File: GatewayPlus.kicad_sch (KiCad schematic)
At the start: 0 parts

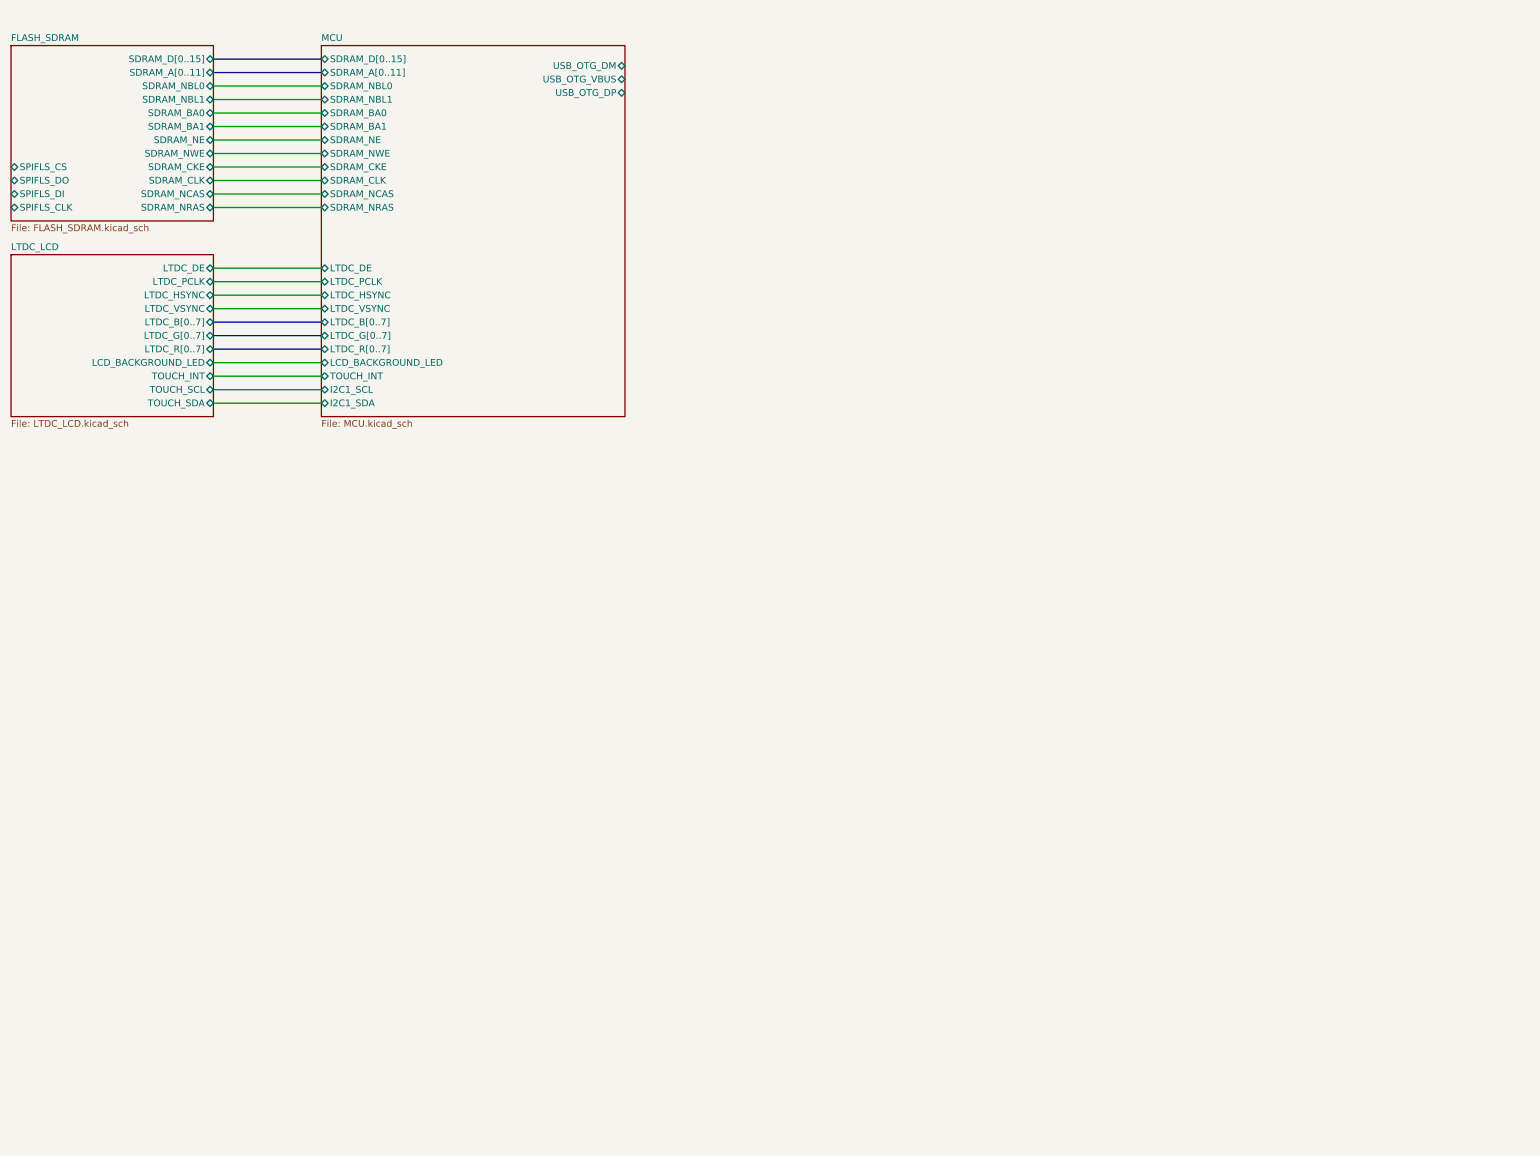
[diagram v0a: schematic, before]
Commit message: Add WiFi block and finished WiFi layout
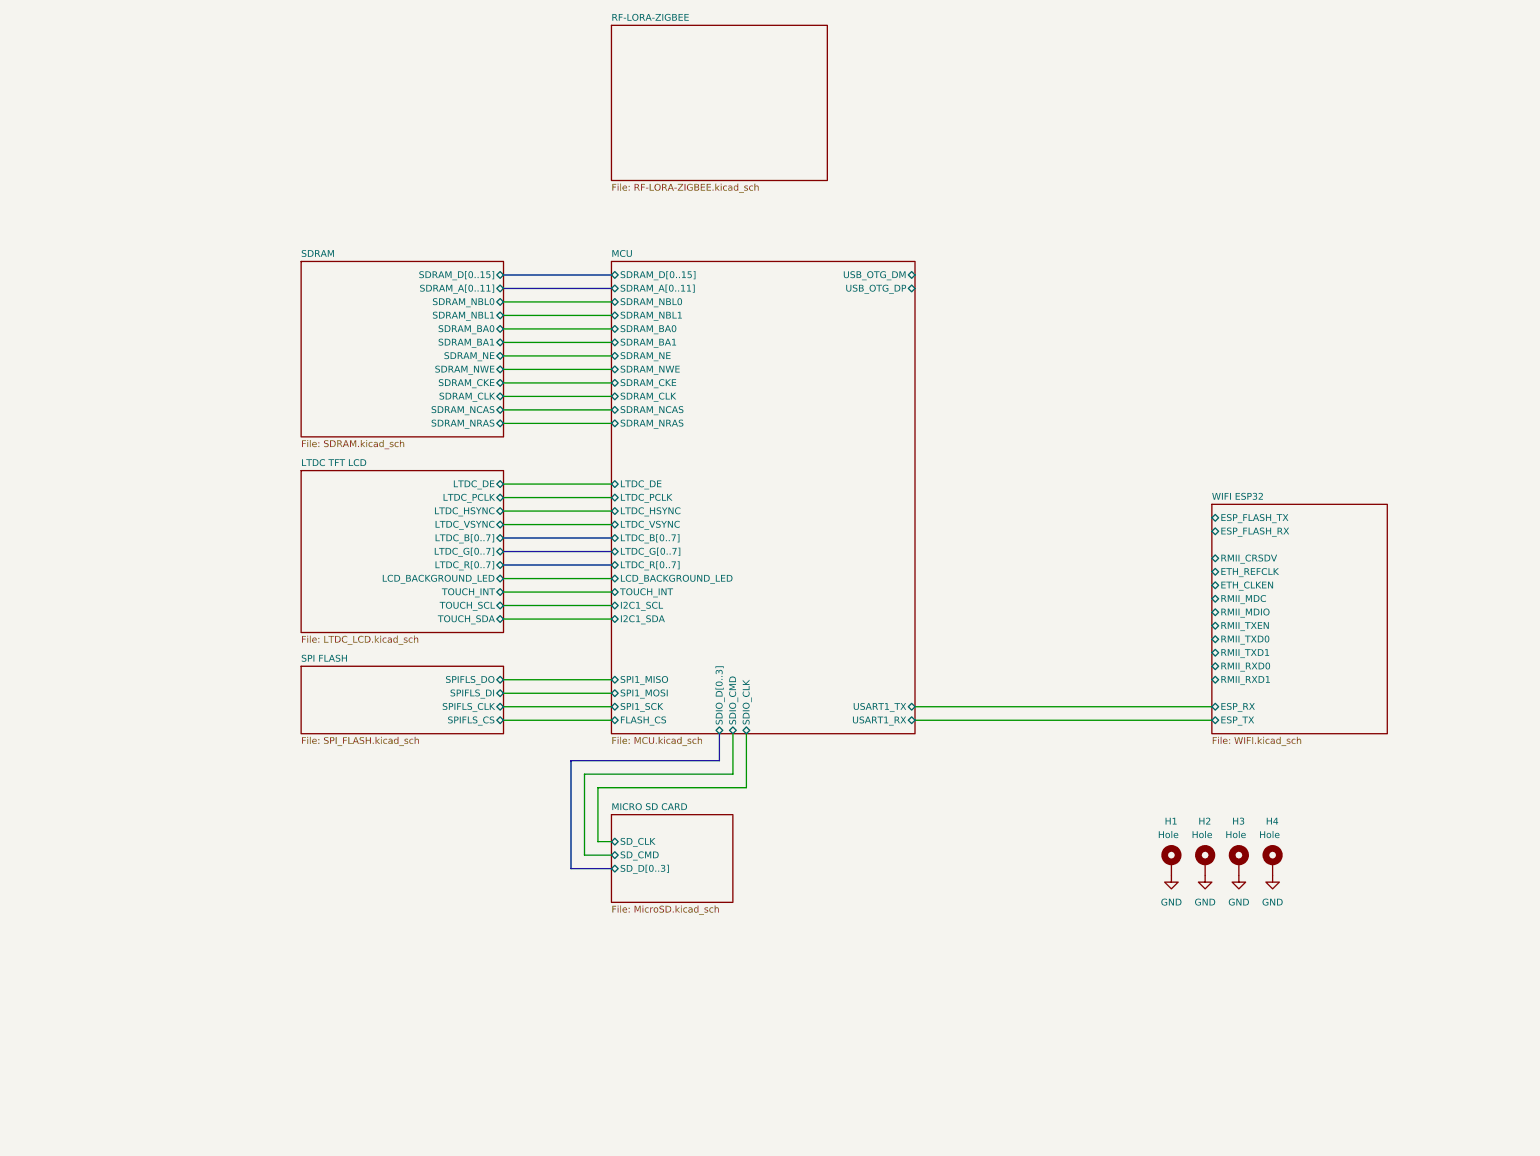
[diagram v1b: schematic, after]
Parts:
- added H1, H2, H3, H4: Hole, MountingHole:MountingHole_3.2mm_M3_Pad_Via, symbol Mechanical:MountingHole_Pad
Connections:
- new net GND: H1.1, H2.1, H3.1, H4.1
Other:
- sheet FLASH_SDRAM renamed SDRAM
- sheet LTDC_LCD renamed LTDC TFT LCD
- added sheet MICRO SD CARD (MicroSD.kicad_sch)
- added sheet RF-LORA-ZIGBEE (RF-LORA-ZIGBEE.kicad_sch)
- added sheet SPI FLASH (SPI_FLASH.kicad_sch)
- added sheet WIFI ESP32 (WIFI.kicad_sch)
- sheet MCU ports: added FLASH_CS, SDIO_CLK, SDIO_CMD, SDIO_D[0..3], SPI1_MISO, SPI1_MOSI, SPI1_SCK, USART1_RX, USART1_TX; removed USB_OTG_VBUS
- sheet SDRAM: file FLASH_SDRAM.kicad_sch -> SDRAM.kicad_sch
- sheet SDRAM ports: added none; removed SPIFLS_CLK, SPIFLS_CS, SPIFLS_DI, SPIFLS_DO

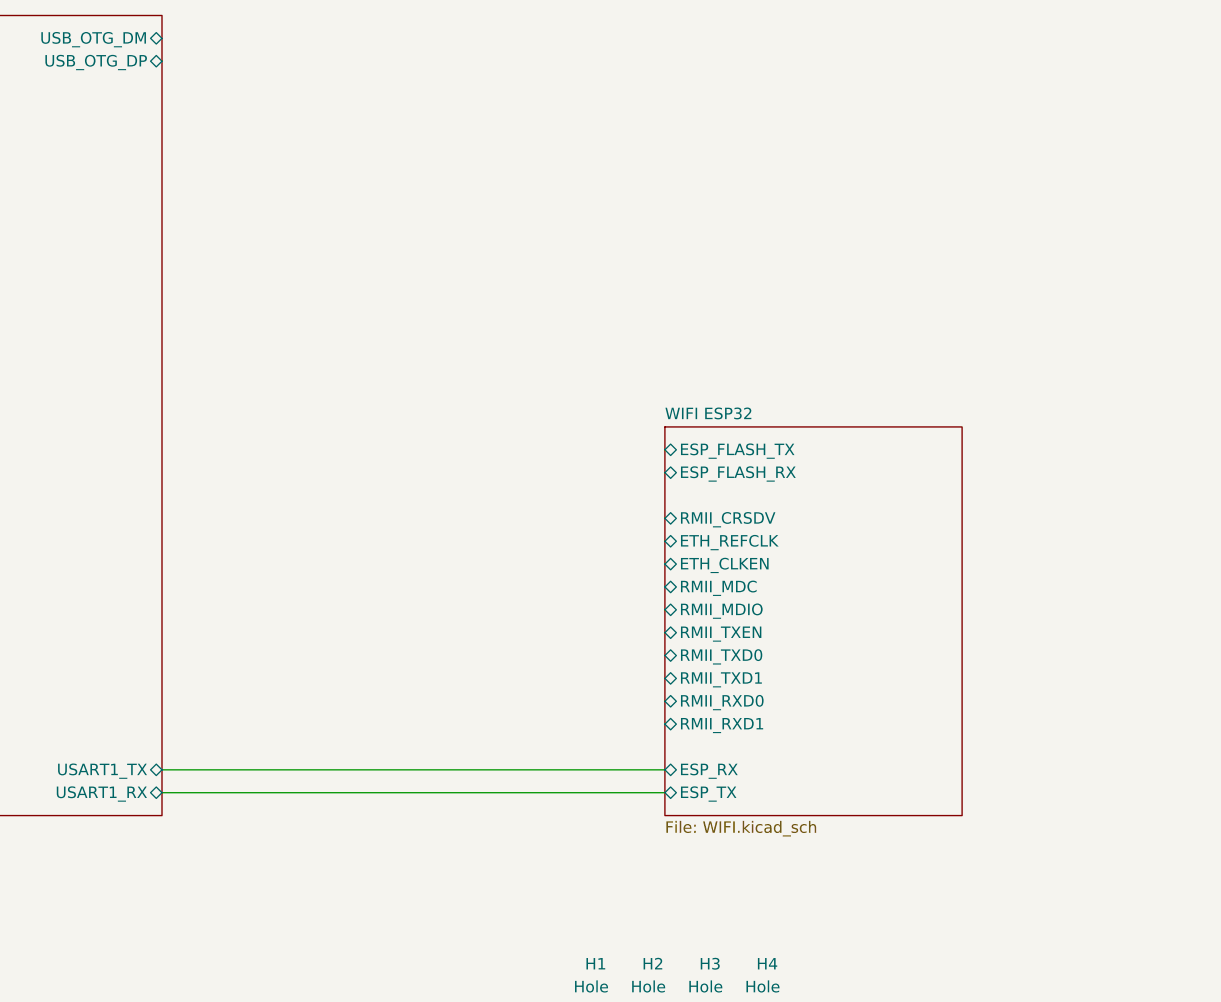
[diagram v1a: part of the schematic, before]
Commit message: Add Ethernet LAN8720 Layout.
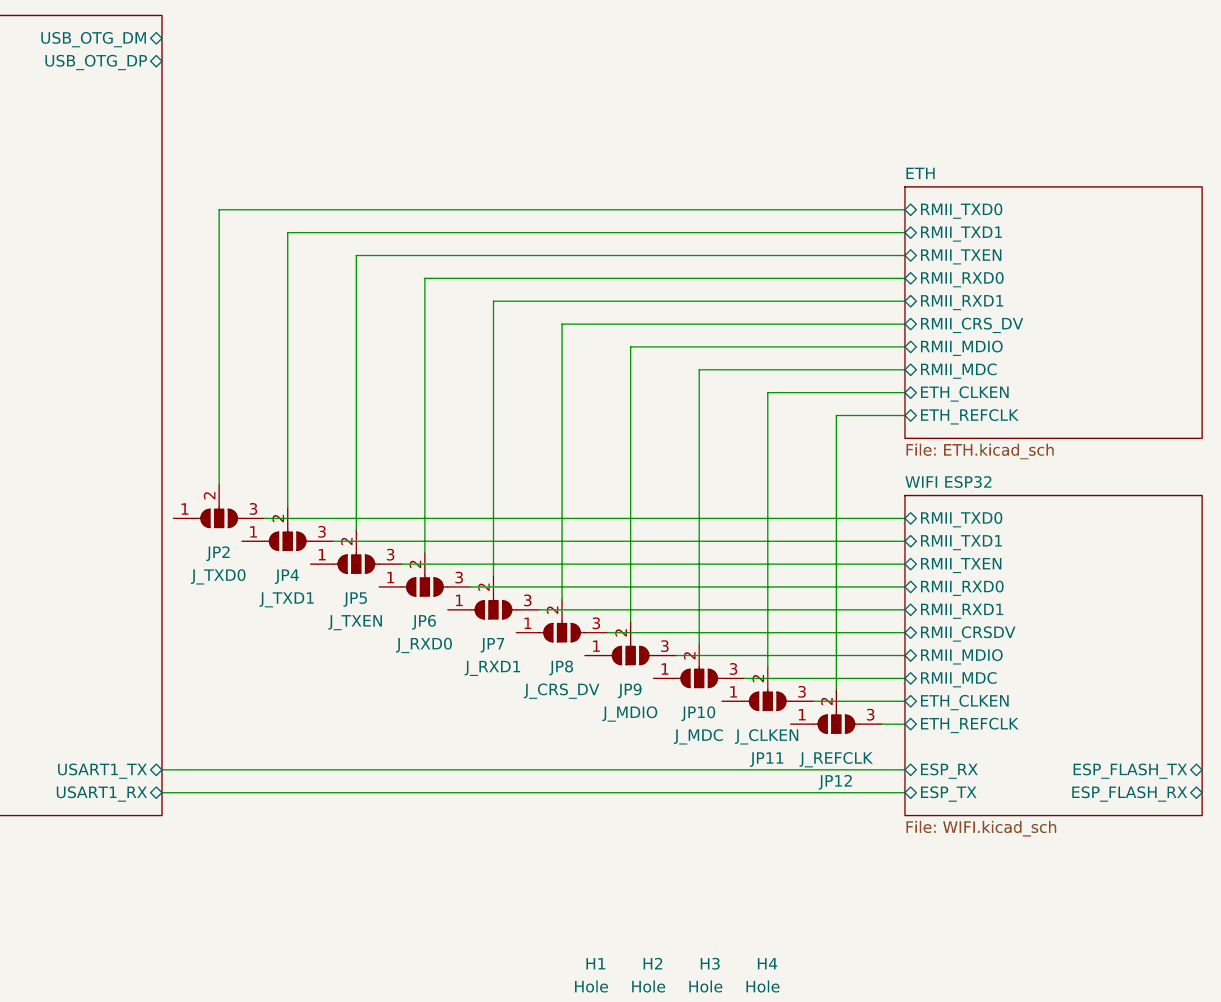
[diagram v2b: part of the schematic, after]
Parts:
- added JP10: J_MDC, Anh_Footprints:Jump3_0603_Open, symbol Jumper:SolderJumper_3_Open
- added JP11: J_CLKEN, Anh_Footprints:Jump3_0603_Open, symbol Jumper:SolderJumper_3_Open
- added JP12: J_REFCLK, Anh_Footprints:Jump3_0603_Open, symbol Jumper:SolderJumper_3_Open
- added JP2: J_TXD0, Anh_Footprints:Jump3_0603_Open, symbol Jumper:SolderJumper_3_Open
- added JP4: J_TXD1, Anh_Footprints:Jump3_0603_Open, symbol Jumper:SolderJumper_3_Open
- added JP5: J_TXEN, Anh_Footprints:Jump3_0603_Open, symbol Jumper:SolderJumper_3_Open
- added JP6: J_RXD0, Anh_Footprints:Jump3_0603_Open, symbol Jumper:SolderJumper_3_Open
- added JP7: J_RXD1, Anh_Footprints:Jump3_0603_Open, symbol Jumper:SolderJumper_3_Open
- added JP8: J_CRS_DV, Anh_Footprints:Jump3_0603_Open, symbol Jumper:SolderJumper_3_Open
- added JP9: J_MDIO, Anh_Footprints:Jump3_0603_Open, symbol Jumper:SolderJumper_3_Open
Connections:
- net WIFI ESP32/ETH_CLKEN: now also JP11.3 (B)
- net WIFI ESP32/ETH_REFCLK: now also JP12.3 (B)
- net WIFI ESP32/RMII_CRSDV: now also JP8.3 (B)
- net WIFI ESP32/RMII_MDC: now also JP10.3 (B)
- net WIFI ESP32/RMII_MDIO: now also JP9.3 (B)
- net WIFI ESP32/RMII_RXD0: now also JP6.3 (B)
- net WIFI ESP32/RMII_RXD1: now also JP7.3 (B)
- net WIFI ESP32/RMII_TXD0: now also JP2.3 (B)
- net WIFI ESP32/RMII_TXD1: now also JP4.3 (B)
- net WIFI ESP32/RMII_TXEN: now also JP5.3 (B)
- new net ETH/ETH_CLKEN: JP11.2 (C)
- new net ETH/ETH_REFCLK: JP12.2 (C)
- new net ETH/RMII_CRS_DV: JP8.2 (C)
- new net ETH/RMII_MDC: JP10.2 (C)
- new net ETH/RMII_MDIO: JP9.2 (C)
- new net ETH/RMII_RXD0: JP6.2 (C)
- new net ETH/RMII_RXD1: JP7.2 (C)
- new net ETH/RMII_TXD0: JP2.2 (C)
- new net ETH/RMII_TXD1: JP4.2 (C)
- new net ETH/RMII_TXEN: JP5.2 (C)
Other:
- added sheet ETH (ETH.kicad_sch)

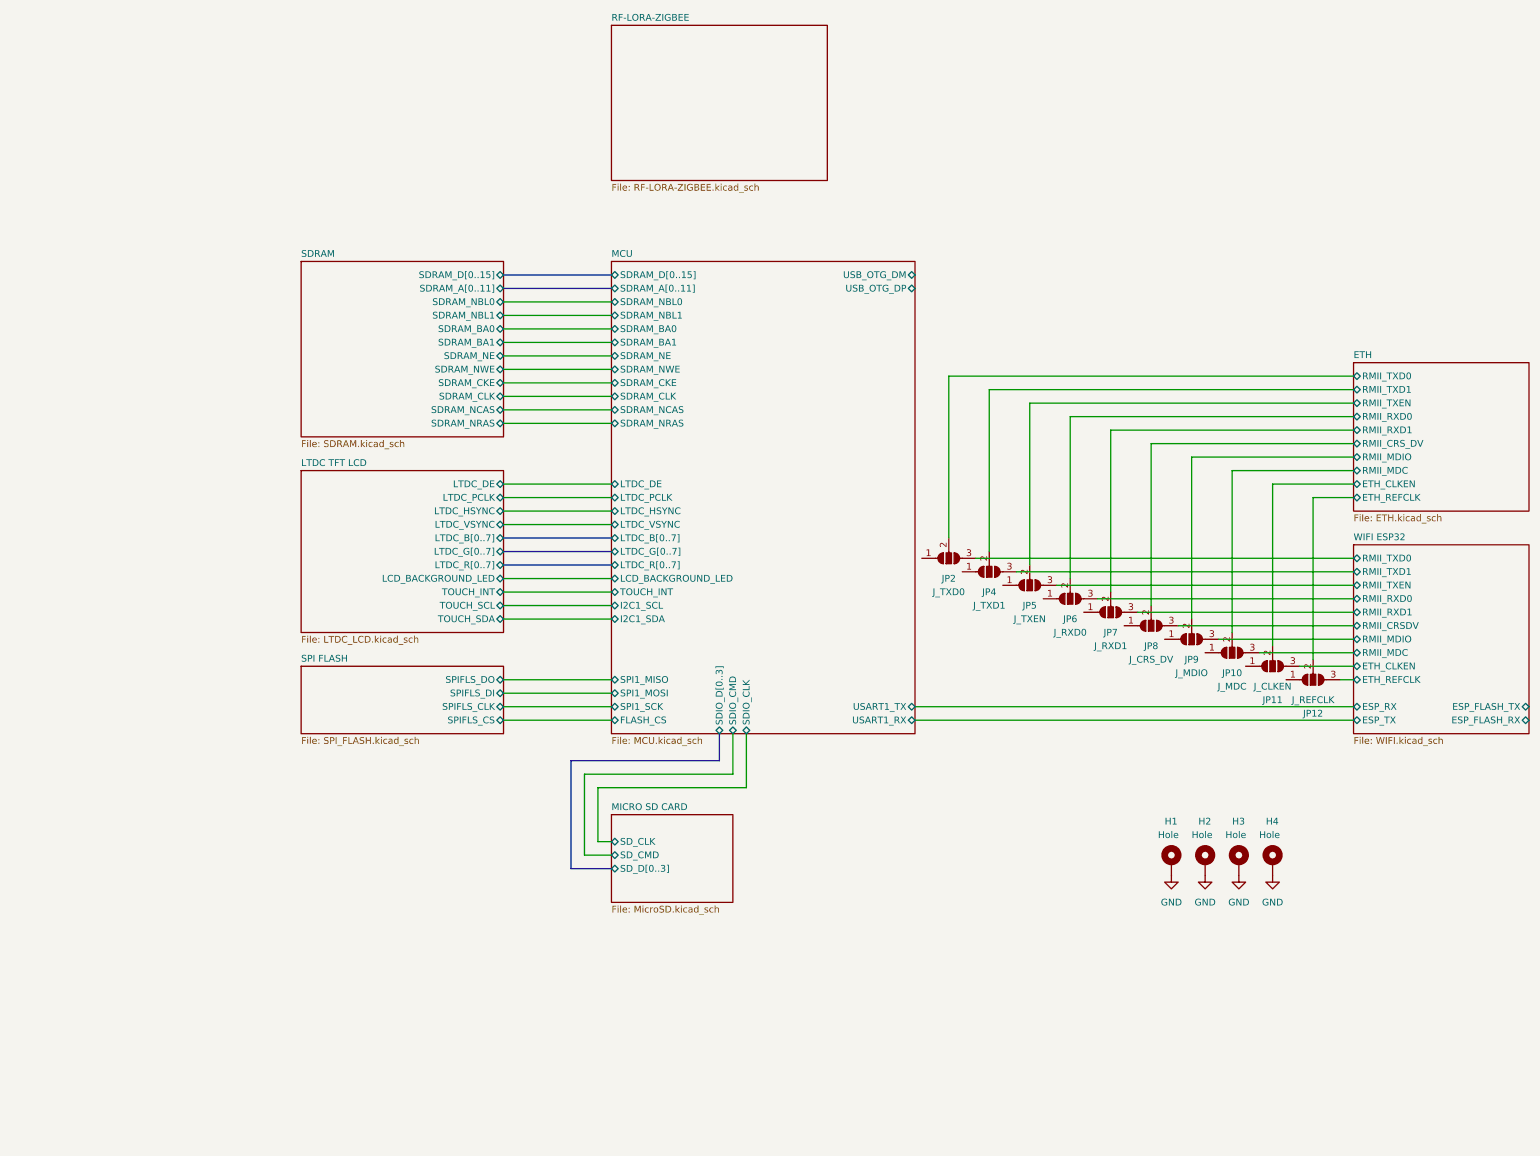
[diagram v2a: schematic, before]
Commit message: Finish Ethernet Layout.
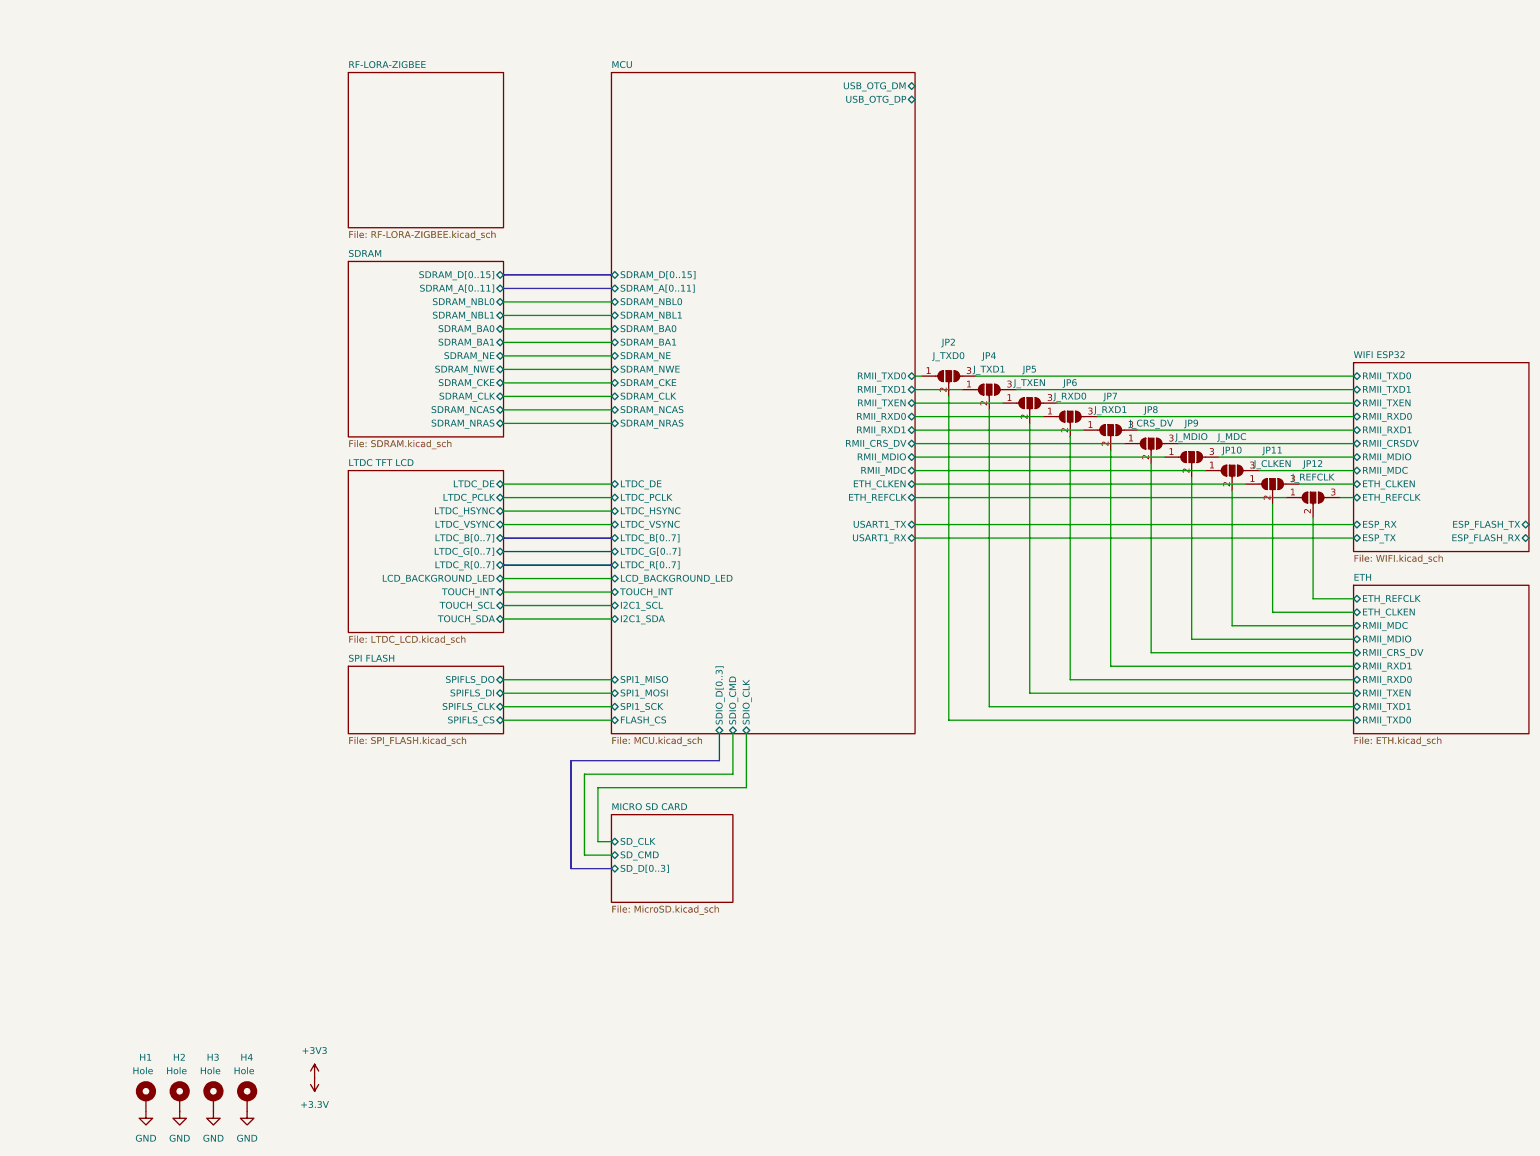
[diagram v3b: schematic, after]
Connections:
- net MCU/ETH_REFCLK: now reaches JP12.1 (A)
- net MCU/RMII_CRS_DV: now reaches JP8.1 (A)
- net MCU/ETH_CLKEN: now reaches JP11.1 (A)
- net MCU/RMII_MDC: now reaches JP10.1 (A)
- net MCU/RMII_TXD1: now reaches JP4.1 (A)
- net MCU/RMII_TXD0: now reaches JP2.1 (A)
- net MCU/RMII_RXD1: now reaches JP7.1 (A)
- net MCU/RMII_TXEN: now reaches JP5.1 (A)
- net MCU/RMII_MDIO: now reaches JP9.1 (A)
- net MCU/RMII_RXD0: now reaches JP6.1 (A)
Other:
- sheet MCU ports: added ETH_CLKEN, ETH_REFCLK, RMII_CRS_DV, RMII_MDC, RMII_MDIO, RMII_RXD0, RMII_RXD1, RMII_TXD0, RMII_TXD1, RMII_TXEN; removed none
- moved on the sheet: H1, H2, H3, H4, JP10, JP11, JP12, JP2, JP4, JP5, JP6, JP7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
